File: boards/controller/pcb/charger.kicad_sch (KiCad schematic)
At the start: 32 parts, among them J4001 Battery, U4001 BQ25792RQMR

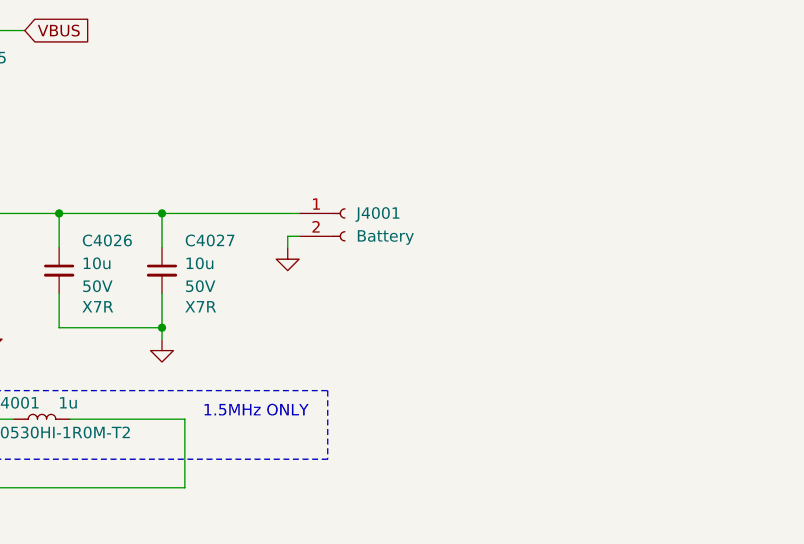
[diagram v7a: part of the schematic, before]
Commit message: controller: pcb: Update schematic
- Add power button pmos gate voltage clamp
- Add TVS diodes on encoders

Signed-off-by: Nicholas Loehrke <nicholasnloehrke@gmail.com>
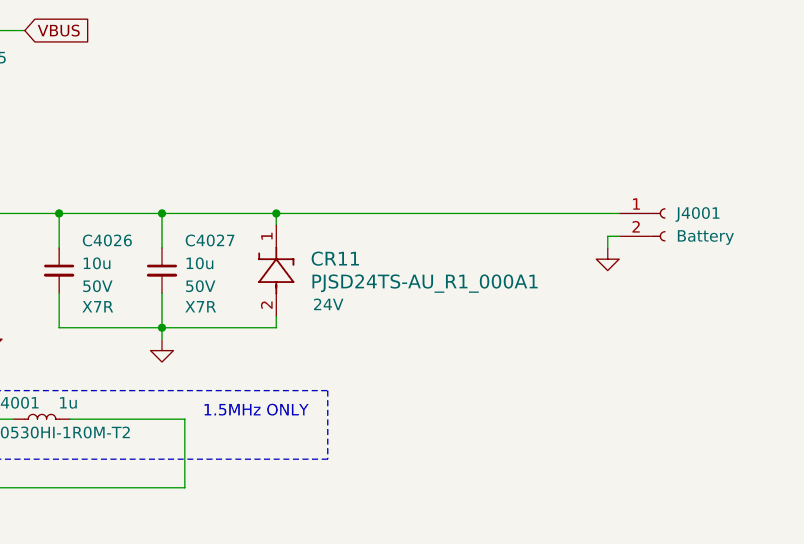
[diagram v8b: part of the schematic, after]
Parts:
- added CR11: PJSD24TS-AU_R1_000A1, CR_SOD-523_PNJ, symbol PJSD24TS-AU_R1_000A1:PJSD24TS-AU_R1_000A1
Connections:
- net GND: now also CR11.2
- net at C4026.1, C4027.1, J4001.1 (Pin_1)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: now also CR11.1
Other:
- moved on the sheet: J4001
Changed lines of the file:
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@@
 	)
 	(junction
+		(at 224.79 74.93)
+		(diameter 0)
+		(color 0 0 0 0)
+	)
+	(junction
 		(at 238.76 113.03)
 		(diameter 0)
@@
 	(wire
 		(pts
+			(xy 224.79 74.93) (xy 224.79 76.2)
+		)
+		(stroke
+			(width 0.508)
+			(type default)
+		)
+	)
+	(wire
+		(pts
 			(xy 114.3 72.39) (xy 114.3 73.66)
 		)
@@
 	(wire
 		(pts
+			(xy 212.09 74.93) (xy 224.79 74.93)
+		)
+		(stroke
+			(width 0.508)
+			(type default)
+		)
+	)
+	(wire
+		(pts
 			(xy 138.43 144.78) (xy 138.43 148.59)
 		)
@@
 	(wire
 		(pts
-			(xy 212.09 74.93) (xy 227.33 74.93)
-		)
-		(stroke
-			(width 0.508)
-			(type default)
-		)
-	)
-	(wire
-		(pts
 			(xy 238.76 113.03) (xy 250.19 113.03)
 		)
@@
 	(wire
 		(pts
+			(xy 212.09 87.63) (xy 224.79 87.63)
+		)
+		(stroke
+			(width 0.508)
+			(type default)
+		)
+	)
+	(wire
+		(pts
 			(xy 212.09 74.93) (xy 212.09 78.74)
 		)
@@
 	(wire
 		(pts
-			(xy 226.06 77.47) (xy 227.33 77.47)
+			(xy 261.62 77.47) (xy 262.89 77.47)
 		)
 		(stroke
@@
 	(wire
 		(pts
-			(xy 226.06 78.74) (xy 226.06 77.47)
+			(xy 261.62 78.74) (xy 261.62 77.47)
 		)
 		(stroke
@@
 	(wire
 		(pts
+			(xy 224.79 87.63) (xy 224.79 86.36)
+		)
+		(stroke
+			(width 0.508)
+			(type default)
+		)
+	)
+	(wire
+		(pts
 			(xy 200.66 83.82) (xy 200.66 87.63)
 		)
@@
 	(wire
 		(pts
+			(xy 224.79 74.93) (xy 262.89 74.93)
+		)
+		(stroke
+			(width 0.508)
+			(type default)
+		)
+	)
+	(wire
+		(pts
 			(xy 74.93 115.57) (xy 74.93 116.84)
 		)
@@
 	(symbol
 		(lib_id "Connector:Conn_01x02_Socket")
-		(at 232.41 74.93 0)
+		(at 267.97 74.93 0)
 		(unit 1)
 		(exclude_from_sim no)
@@
 		(fields_autoplaced yes)
 		(property "Reference" "J4001"
-			(at 233.68 74.9299 0)
+			(at 269.24 74.9299 0)
 			(effects
 				(font
@@
 		)
 		(property "Value" "Battery"
-			(at 233.68 77.4699 0)
+			(at 269.24 77.4699 0)
 			(effects
 				(font
@@
 		)
 		(property "Footprint" ""
-			(at 232.41 74.93 0)
+			(at 267.97 74.93 0)
 			(effects
 				(font
@@
 		)
 		(property "Datasheet" "~"
-			(at 232.41 74.93 0)
+			(at 267.97 74.93 0)
 			(effects
 				(font
@@
 		)
 		(property "Description" "Generic connector, single row, 01x02, script generated"
-			(at 232.41 74.93 0)
+			(at 267.97 74.93 0)
 			(effects
 				(font
@@
 	(symbol
 		(lib_id "power:GND")
-		(at 226.06 78.74 0)
+		(at 261.62 78.74 0)
 		(unit 1)
 		(exclude_from_sim no)
@@
 		(fields_autoplaced yes)
 		(property "Reference" "#PWR04011"
-			(at 226.06 85.09 0)
+			(at 261.62 85.09 0)
 			(effects
 				(font
@@
 		)
 		(property "Value" "GND"
-			(at 226.06 83.82 0)
+			(at 261.62 83.82 0)
 			(effects
 				(font
@@
 		)
 		(property "Footprint" ""
-			(at 226.06 78.74 0)
+			(at 261.62 78.74 0)
 			(effects
 				(font
@@
 		)
 		(property "Datasheet" ""
-			(at 226.06 78.74 0)
+			(at 261.62 78.74 0)
 			(effects
 				(font
@@
 		)
 		(property "Description" "Power symbol creates a global label with name \"GND\" , ground"
-			(at 226.06 78.74 0)
+			(at 261.62 78.74 0)
 			(effects
 				(font
@@
 					(unit 1)
 				)
+			)
+		)
+	)
+	(symbol
+		(lib_id "PJSD24TS-AU_R1_000A1:PJSD24TS-AU_R1_000A1")
+		(at 224.79 86.36 90)
+		(unit 1)
+		(exclude_from_sim no)
+		(in_bom yes)
+		(on_board yes)
+		(dnp no)
+		(property "Reference" "CR11"
+			(at 228.6 80.0099 90)
+			(effects
+				(font
+					(size 1.524 1.524)
+				)
+				(justify right)
+			)
+		)
+		(property "Value" "PJSD24TS-AU_R1_000A1"
+			(at 228.6 82.5499 90)
+			(effects
+				(font
+					(size 1.524 1.524)
+				)
+				(justify right)
+			)
+		)
+		(property "Footprint" "CR_SOD-523_PNJ"
+			(at 224.79 86.36 0)
+			(effects
+				(font
+					(size 1.27 1.27)
+					(italic yes)
+				)
+				(hide yes)
+			)
+		)
+		(property "Datasheet" "PJSD24TS-AU_R1_000A1"
+			(at 224.79 86.36 0)
+			(effects
+				(font
+					(size 1.27 1.27)
+					(italic yes)
+				)
+				(hide yes)
+			)
+		)
+		(property "Description" ""
+			(at 224.79 86.36 0)
+			(effects
+				(font
+					(size 1.27 1.27)
+				)
+				(hide yes)
+			)
+		)
+		(property "MPN" ""
+			(at 224.79 86.36 0)
+			(effects
+				(font
+					(size 1.27 1.27)
+				)
+			)
+		)
+		(property "TCC" ""
+			(at 224.79 86.36 0)
+			(effects
+				(font
+					(size 1.27 1.27)
+				)
+			)
+		)
+		(property "Tolerance" ""
+			(at 224.79 86.36 0)
+			(effects
+				(font
+					(size 1.27 1.27)
+				)
+			)
+		)
+		(property "Voltage" "24V"
+			(at 228.854 85.09 90)
+			(effects
+				(font
+					(size 1.27 1.27)
+				)
+				(justify right)
+			)
+		)
+		(property "Package" ""
+			(at 224.79 86.36 0)
+			(effects
+				(font
+					(size 1.27 1.27)
+				)
+			)
+		)
+		(pin "2"
+		)
+		(pin "1"
+		)
+		(instances
+			(project "controller"
+				(path "/5caba13a-97ae-46d4-856f-900b12012fd8/abd51820-7208-42b0-b9f8-9a931d762a6f"
+					(reference "CR11")
+					(unit 1)
+				)
